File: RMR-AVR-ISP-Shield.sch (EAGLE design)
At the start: 31 parts, among them IC1 AVR-MEGA-PZIF_SOCKET, J1 AVR_SPI_PRG_6PTH, U1 ARDUINO_SHIELDLABEL, X1 16.00MHz, Y1 16MHz

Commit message: Add files via upload
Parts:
- added C4: 10uF, SparkFun-Capacitors:10UF-POLAR-RADIAL-2.5MM-25V-20%
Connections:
- net GND: now also C4.-
- net RES: now also C4.+
- net RX: no longer IC1.PD1(TXD)
- net TX: no longer IC1.PD0(RXD)
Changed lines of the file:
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@@
 <part name="SW2" library="adafruit" library_urn="urn:adsk.eagle:library:420" deviceset="SWITCH_PUSHBUTTON" device="EVQ-PE" package3d_urn="urn:adsk.eagle:package:6240957/1"/>
 <part name="GND10" library="SparkFun" deviceset="GND" device=""/>
+<part name="C4" library="SparkFun-Capacitors" library_urn="urn:adsk.eagle:library:510" deviceset="10UF-POLAR" device="-RADIAL-2.5MM-25V-20%" package3d_urn="urn:adsk.eagle:package:37423/1" value="10uF"/>
+<part name="GND13" library="SparkFun" deviceset="GND" device=""/>
 </parts>
 <sheets>
@@
 <attribute name="VALUE" x="88.9" y="104.14" size="1.778" layer="96" rot="R270"/>
 </instance>
+<instance part="C4" gate="G$1" x="5.08" y="170.18" smashed="yes">
+<attribute name="NAME" x="6.096" y="170.815" size="1.778" layer="95" font="vector"/>
+<attribute name="VALUE" x="6.096" y="165.989" size="1.778" layer="96" font="vector"/>
+</instance>
+<instance part="GND13" gate="1" x="5.08" y="160.02" smashed="yes">
+<attribute name="VALUE" x="2.54" y="157.48" size="1.778" layer="96"/>
+</instance>
 </instances>
 <busses>
@@
 <wire x1="99.06" y1="101.6" x2="93.98" y2="101.6" width="0.1524" layer="91"/>
 </segment>
+<segment>
+<pinref part="C4" gate="G$1" pin="-"/>
+<wire x1="5.08" y1="165.1" x2="5.08" y2="162.56" width="0.1524" layer="91"/>
+<pinref part="GND13" gate="1" pin="GND"/>
+</segment>
 </net>
 <net name="5V" class="0">
@@
 <pinref part="J8" gate="G$1" pin="1"/>
 </segment>
-<segment>
-<wire x1="99.06" y1="60.96" x2="109.22" y2="60.96" width="0.1524" layer="91"/>
-<label x="104.14" y="60.96" size="1.778" layer="95"/>
-<pinref part="IC1" gate="G$1" pin="PD1(TXD)"/>
-</segment>
 </net>
 <net name="TX" class="0">
@@
 <pinref part="U1" gate="G$1" pin="TX"/>
 <pinref part="J7" gate="G$1" pin="1"/>
-</segment>
-<segment>
-<wire x1="99.06" y1="63.5" x2="109.22" y2="63.5" width="0.1524" layer="91"/>
-<label x="104.14" y="63.5" size="1.778" layer="95"/>
-<pinref part="IC1" gate="G$1" pin="PD0(RXD)"/>
 </segment>
 </net>
@@
 <label x="119.38" y="101.6" size="1.016" layer="95" xref="yes"/>
 </segment>
-</net>
+<segment>
+<pinref part="C4" gate="G$1" pin="+"/>
+<wire x1="5.08" y1="172.72" x2="5.08" y2="175.26" width="0.1524" layer="91"/>
+<label x="5.08" y="172.72" size="1.778" layer="95" rot="R90"/>
+</segment>
+</net>

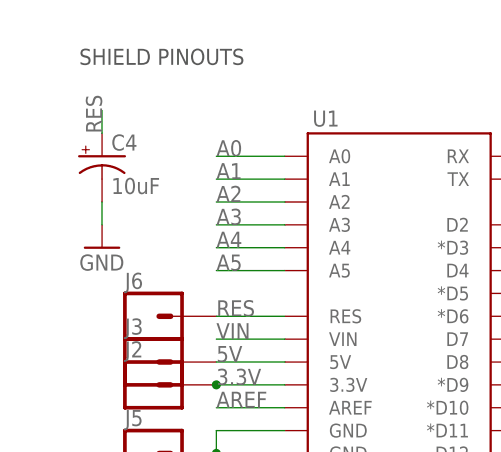
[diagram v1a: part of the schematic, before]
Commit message: Add files via upload
changed reset capacitor
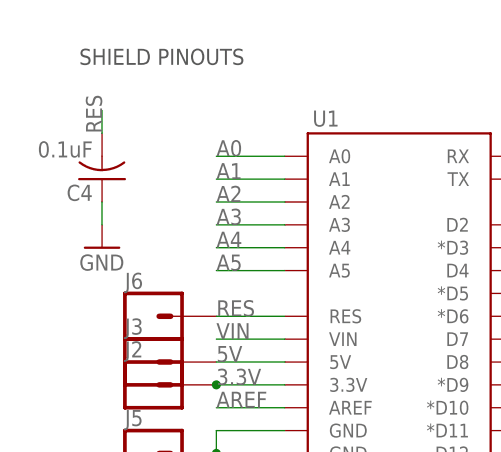
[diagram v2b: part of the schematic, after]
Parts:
- C4: value 10uF -> 0.1uF; device SparkFun-Capacitors:10UF-POLAR-RADIAL-2.5MM-25V-20% -> adafruit:C-US025-024X044
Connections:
- net GND: now also C4.1; no longer C4.-
- net RES: now also C4.2; no longer C4.+
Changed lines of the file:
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@@
 <grid distance="0.1" unitdist="inch" unit="inch" style="lines" multiple="1" display="no" altdistance="0.01" altunitdist="inch" altunit="inch"/>
 <layers>
-<layer number="1" name="Top" color="4" fill="1" visible="no" active="no"/>
-<layer number="2" name="Route2" color="1" fill="3" visible="no" active="no"/>
-<layer number="3" name="Route3" color="4" fill="3" visible="no" active="no"/>
-<layer number="4" name="Route4" color="1" fill="4" visible="no" active="no"/>
-<layer number="5" name="Route5" color="4" fill="4" visible="no" active="no"/>
-<layer number="6" name="Route6" color="1" fill="8" visible="no" active="no"/>
-<layer number="7" name="Route7" color="4" fill="8" visible="no" active="no"/>
-<layer number="8" name="Route8" color="1" fill="2" visible="no" active="no"/>
-<layer number="9" name="Route9" color="4" fill="2" visible="no" active="no"/>
-<layer number="10" name="Route10" color="1" fill="7" visible="no" active="no"/>
-<layer number="11" name="Route11" color="4" fill="7" visible="no" active="no"/>
-<layer number="12" name="Route12" color="1" fill="5" visible="no" active="no"/>
-<layer number="13" name="Route13" color="4" fill="5" visible="no" active="no"/>
-<layer number="14" name="Route14" color="1" fill="6" visible="no" active="no"/>
-<layer number="15" name="Route15" color="4" fill="6" visible="no" active="no"/>
-<layer number="16" name="Bottom" color="1" fill="1" visible="no" active="no"/>
-<layer number="17" name="Pads" color="2" fill="1" visible="no" active="no"/>
-<layer number="18" name="Vias" color="2" fill="1" visible="no" active="no"/>
-<layer number="19" name="Unrouted" color="6" fill="1" visible="no" active="no"/>
-<layer number="20" name="Dimension" color="6" fill="1" visible="no" active="no"/>
-<layer number="21" name="tPlace" color="16" fill="1" visible="no" active="no"/>
-<layer number="22" name="bPlace" color="14" fill="1" visible="no" active="no"/>
-<layer number="23" name="tOrigins" color="15" fill="1" visible="no" active="no"/>
-<layer number="24" name="bOrigins" color="15" fill="1" visible="no" active="no"/>
-<layer number="25" name="tNames" color="7" fill="1" visible="no" active="no"/>
-<layer number="26" name="bNames" color="7" fill="1" visible="no" active="no"/>
-<layer number="27" name="tValues" color="7" fill="1" visible="no" active="no"/>
-<layer number="28" name="bValues" color="7" fill="1" visible="no" active="no"/>
+<layer number="1" name="Top" color="4" fill="1" visible="yes" active="no"/>
+<layer number="2" name="Route2" color="1" fill="3" visible="yes" active="no"/>
+<layer number="3" name="Route3" color="4" fill="3" visible="yes" active="no"/>
+<layer number="4" name="Route4" color="1" fill="4" visible="yes" active="no"/>
+<layer number="5" name="Route5" color="4" fill="4" visible="yes" active="no"/>
+<layer number="6" name="Route6" color="1" fill="8" visible="yes" active="no"/>
+<layer number="7" name="Route7" color="4" fill="8" visible="yes" active="no"/>
+<layer number="8" name="Route8" color="1" fill="2" visible="yes" active="no"/>
+<layer number="9" name="Route9" color="4" fill="2" visible="yes" active="no"/>
+<layer number="10" name="Route10" color="1" fill="7" visible="yes" active="no"/>
+<layer number="11" name="Route11" color="4" fill="7" visible="yes" active="no"/>
+<layer number="12" name="Route12" color="1" fill="5" visible="yes" active="no"/>
+<layer number="13" name="Route13" color="4" fill="5" visible="yes" active="no"/>
+<layer number="14" name="Route14" color="1" fill="6" visible="yes" active="no"/>
+<layer number="15" name="Route15" color="4" fill="6" visible="yes" active="no"/>
+<layer number="16" name="Bottom" color="1" fill="1" visible="yes" active="no"/>
+<layer number="17" name="Pads" color="2" fill="1" visible="yes" active="no"/>
+<layer number="18" name="Vias" color="2" fill="1" visible="yes" active="no"/>
+<layer number="19" name="Unrouted" color="6" fill="1" visible="yes" active="no"/>
+<layer number="20" name="Dimension" color="6" fill="1" visible="yes" active="no"/>
+<layer number="21" name="tPlace" color="16" fill="1" visible="yes" active="no"/>
+<layer number="22" name="bPlace" color="14" fill="1" visible="yes" active="no"/>
+<layer number="23" name="tOrigins" color="15" fill="1" visible="yes" active="no"/>
+<layer number="24" name="bOrigins" color="15" fill="1" visible="yes" active="no"/>
+<layer number="25" name="tNames" color="7" fill="1" visible="yes" active="no"/>
+<layer number="26" name="bNames" color="7" fill="1" visible="yes" active="no"/>
+<layer number="27" name="tValues" color="7" fill="1" visible="yes" active="no"/>
+<layer number="28" name="bValues" color="7" fill="1" visible="yes" active="no"/>
 <layer number="29" name="tStop" color="7" fill="3" visible="no" active="no"/>
 <layer number="30" name="bStop" color="7" fill="6" visible="no" active="no"/>
@@
 <layer number="35" name="tGlue" color="7" fill="4" visible="no" active="no"/>
 <layer number="36" name="bGlue" color="7" fill="5" visible="no" active="no"/>
-<layer number="37" name="tTest" color="7" fill="1" visible="no" active="no"/>
-<layer number="38" name="bTest" color="7" fill="1" visible="no" active="no"/>
+<layer number="37" name="tTest" color="7" fill="1" visible="yes" active="no"/>
+<layer number="38" name="bTest" color="7" fill="1" visible="yes" active="no"/>
 <layer number="39" name="tKeepout" color="4" fill="11" visible="no" active="no"/>
 <layer number="40" name="bKeepout" color="1" fill="11" visible="no" active="no"/>
@@
 <layer number="44" name="Drills" color="7" fill="1" visible="no" active="no"/>
 <layer number="45" name="Holes" color="7" fill="1" visible="no" active="no"/>
-<layer number="46" name="Milling" color="3" fill="1" visible="no" active="no"/>
-<layer number="47" name="Measures" color="7" fill="1" visible="no" active="no"/>
-<layer number="48" name="Document" color="7" fill="1" visible="no" active="no"/>
-<layer number="49" name="Reference" color="13" fill="1" visible="no" active="no"/>
-<layer number="50" name="dxf" color="7" fill="1" visible="no" active="no"/>
-<layer number="51" name="tDocu" color="30" fill="1" visible="no" active="no"/>
-<layer number="52" name="bDocu" color="7" fill="1" visible="no" active="no"/>
-<layer number="53" name="tGND_GNDA" color="7" fill="9" visible="no" active="no"/>
-<layer number="54" name="bGND_GNDA" color="1" fill="9" visible="no" active="no"/>
-<layer number="56" name="wert" color="7" fill="1" visible="no" active="no"/>
-<layer number="57" name="tCAD" color="7" fill="1" visible="no" active="no"/>
-<layer number="59" name="tCarbon" color="7" fill="1" visible="no" active="no"/>
-<layer number="60" name="bCarbon" color="7" fill="1" visible="no" active="no"/>
+<layer number="46" name="Milling" color="3" fill="1" visible="yes" active="no"/>
+<layer number="47" name="Measures" color="7" fill="1" visible="yes" active="no"/>
+<layer number="48" name="Document" color="7" fill="1" visible="yes" active="no"/>
+<layer number="49" name="Reference" color="13" fill="1" visible="yes" active="no"/>
+<layer number="50" name="dxf" color="7" fill="1" visible="yes" active="no"/>
+<layer number="51" name="tDocu" color="30" fill="1" visible="yes" active="no"/>
+<layer number="52" name="bDocu" color="7" fill="1" visible="yes" active="no"/>
+<layer number="53" name="tGND_GNDA" color="7" fill="9" visible="yes" active="no"/>
+<layer number="54" name="bGND_GNDA" color="1" fill="9" visible="yes" active="no"/>
+<layer number="56" name="wert" color="7" fill="1" visible="yes" active="no"/>
+<layer number="57" name="tCAD" color="7" fill="1" visible="yes" active="no"/>
+<layer number="59" name="tCarbon" color="7" fill="1" visible="yes" active="no"/>
+<layer number="60" name="bCarbon" color="7" fill="1" visible="yes" active="no"/>
 <layer number="88" name="SimResults" color="9" fill="1" visible="yes" active="yes"/>
 <layer number="89" name="SimProbes" color="9" fill="1" visible="yes" active="yes"/>
@@
 <part name="SW2" library="adafruit" library_urn="urn:adsk.eagle:library:420" deviceset="SWITCH_PUSHBUTTON" device="EVQ-PE" package3d_urn="urn:adsk.eagle:package:6240957/1"/>
 <part name="GND10" library="SparkFun" deviceset="GND" device=""/>
-<part name="C4" library="SparkFun-Capacitors" library_urn="urn:adsk.eagle:library:510" deviceset="10UF-POLAR" device="-RADIAL-2.5MM-25V-20%" package3d_urn="urn:adsk.eagle:package:37423/1" value="10uF"/>
 <part name="GND13" library="SparkFun" deviceset="GND" device=""/>
+<part name="C4" library="adafruit" library_urn="urn:adsk.eagle:library:420" deviceset="C-US" device="025-024X044" package3d_urn="urn:adsk.eagle:package:6240324/1" value="0.1uF"/>
 </parts>
 <sheets>
@@
 <attribute name="VALUE" x="88.9" y="104.14" size="1.778" layer="96" rot="R270"/>
 </instance>
-<instance part="C4" gate="G$1" x="5.08" y="170.18" smashed="yes">
-<attribute name="NAME" x="6.096" y="170.815" size="1.778" layer="95" font="vector"/>
-<attribute name="VALUE" x="6.096" y="165.989" size="1.778" layer="96" font="vector"/>
-</instance>
 <instance part="GND13" gate="1" x="5.08" y="160.02" smashed="yes">
 <attribute name="VALUE" x="2.54" y="157.48" size="1.778" layer="96"/>
+</instance>
+<instance part="C4" gate="G$1" x="5.08" y="167.64" smashed="yes" rot="R180">
+<attribute name="NAME" x="4.064" y="167.005" size="1.778" layer="95" rot="R180"/>
+<attribute name="VALUE" x="4.064" y="171.831" size="1.778" layer="96" rot="R180"/>
 </instance>
 </instances>
@@
 </segment>
 <segment>
-<pinref part="C4" gate="G$1" pin="-"/>
 <wire x1="5.08" y1="165.1" x2="5.08" y2="162.56" width="0.1524" layer="91"/>
 <pinref part="GND13" gate="1" pin="GND"/>
+<pinref part="C4" gate="G$1" pin="1"/>
 </segment>
 </net>
@@
 </segment>
 <segment>
-<pinref part="C4" gate="G$1" pin="+"/>
 <wire x1="5.08" y1="172.72" x2="5.08" y2="175.26" width="0.1524" layer="91"/>
 <label x="5.08" y="172.72" size="1.778" layer="95" rot="R90"/>
-</segment>
-</net>
+<pinref part="C4" gate="G$1" pin="2"/>
+</segment>
+</net>

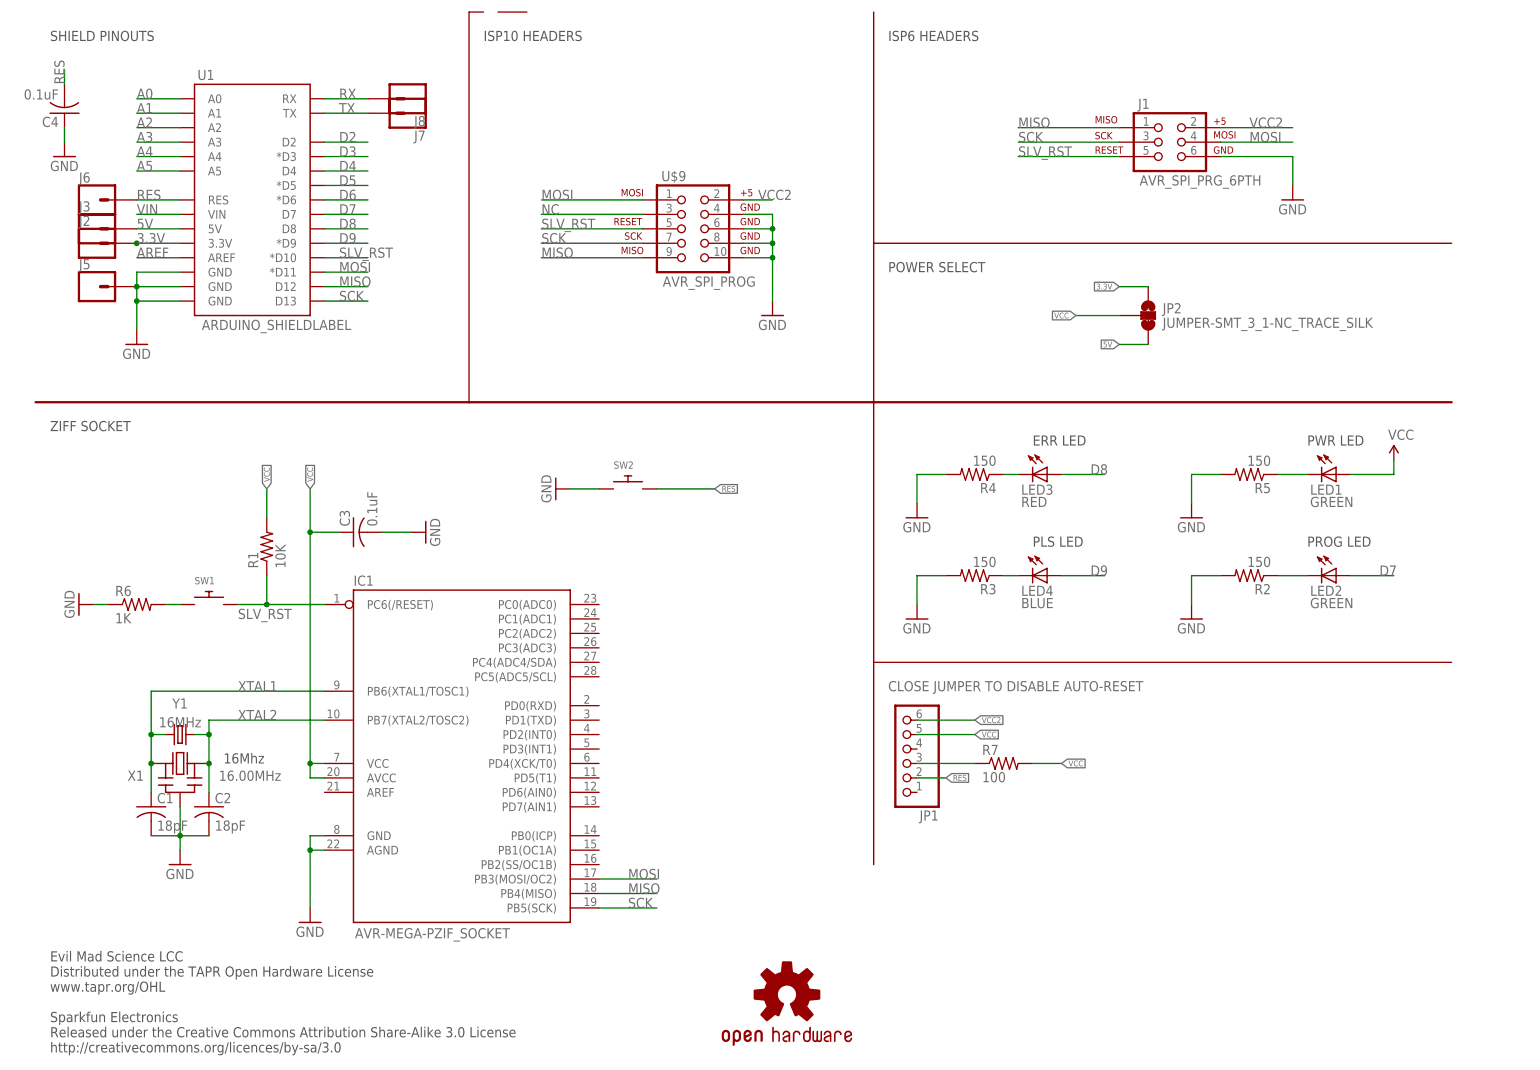
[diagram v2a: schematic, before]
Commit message: Add files via upload
added jumper to the reset capacitor for UNO / 328p based Arduinos.
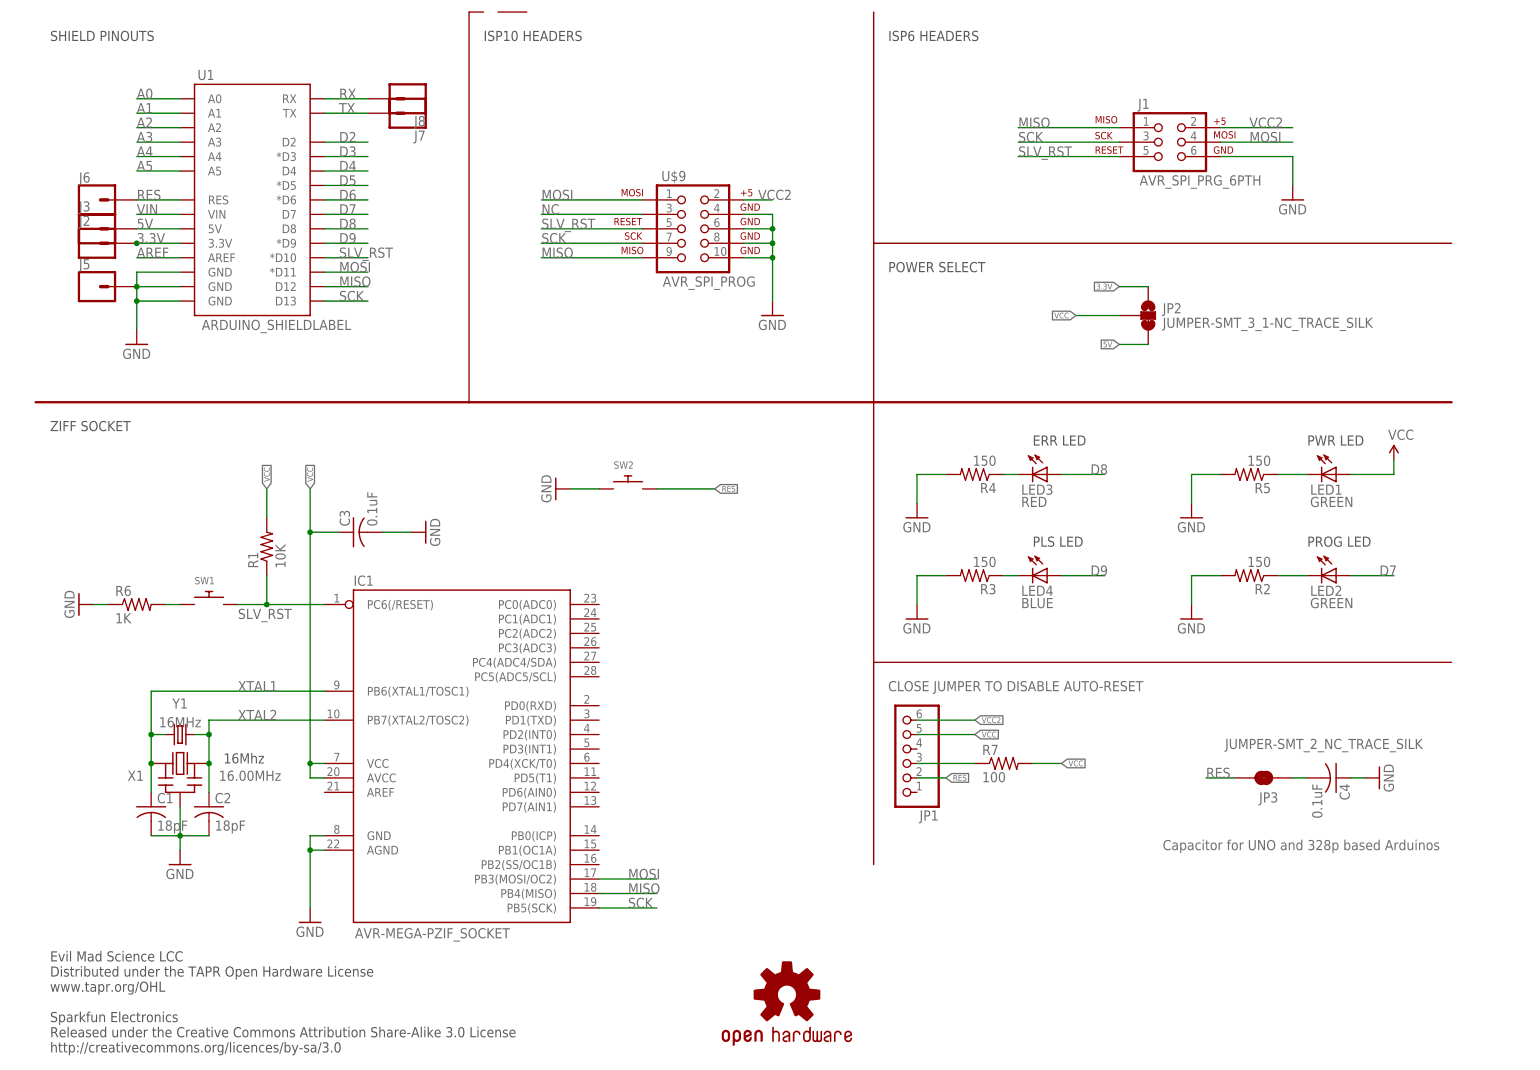
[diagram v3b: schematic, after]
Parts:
- added JP3: JUMPER-SMT_2_NC_TRACE_SILK, SparkFun-Jumpers:JUMPER-SMT_2_NC_TRACE_SILK
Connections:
- new net N$7: C4.2, JP3.1
- net RES: now also JP3.2; no longer C4.2
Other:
- note added: "Capacitor for UNO and 328p based Arduinos"
- moved on the sheet: C4
